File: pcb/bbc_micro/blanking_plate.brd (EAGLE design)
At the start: 66 x 45.5 mm, 0 parts

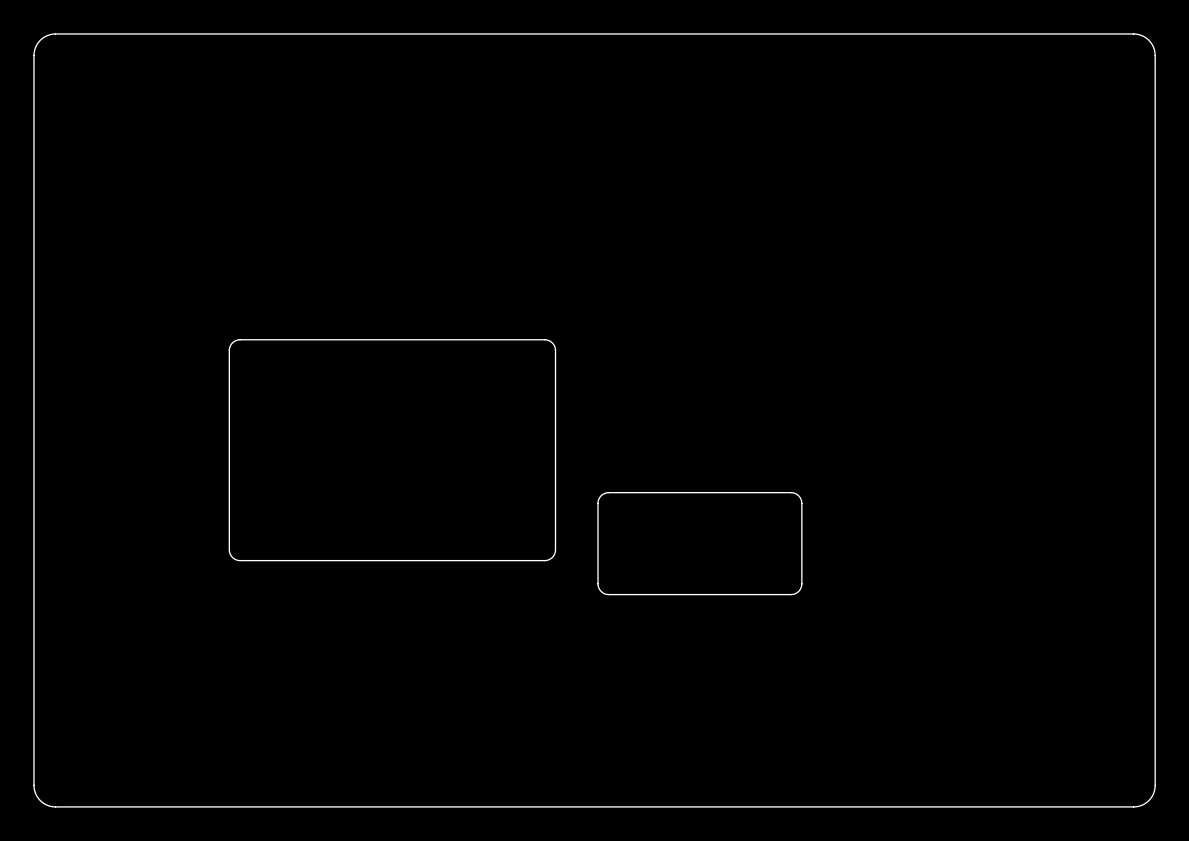
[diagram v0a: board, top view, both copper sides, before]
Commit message: added more caps
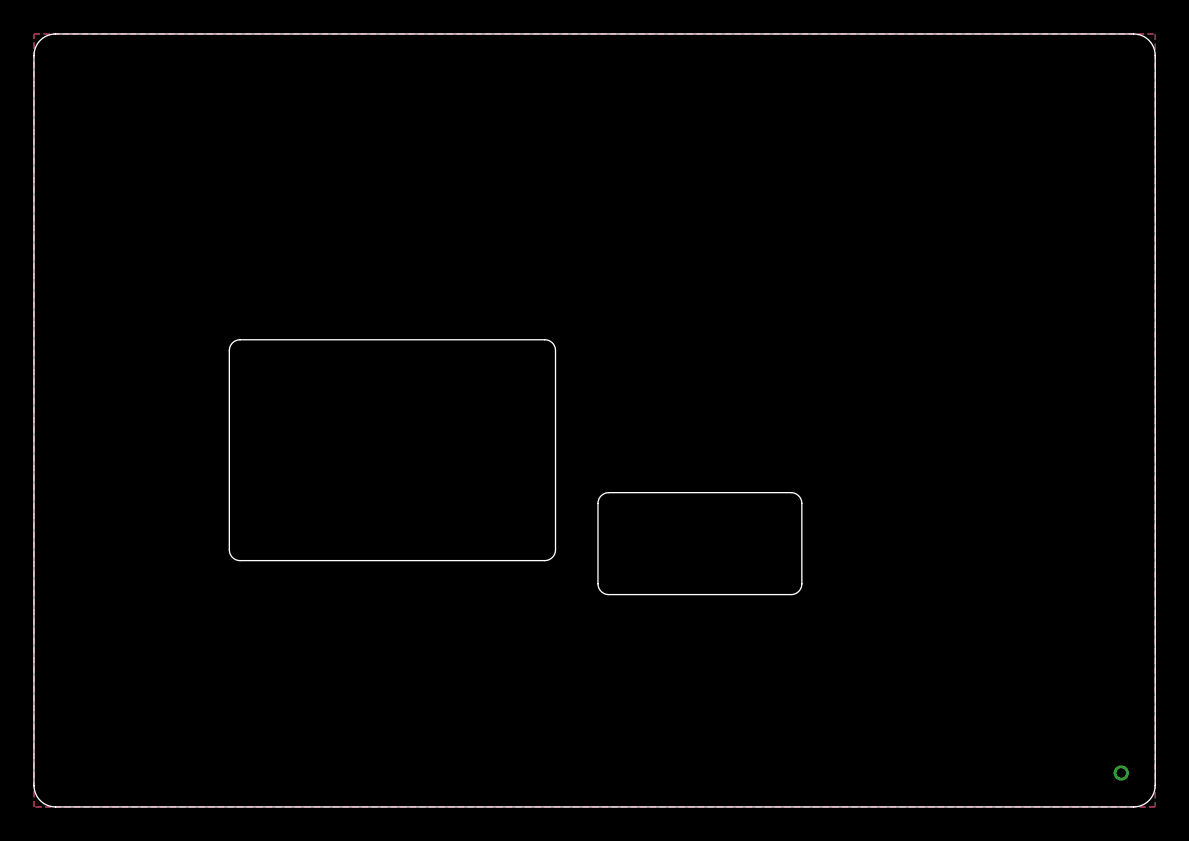
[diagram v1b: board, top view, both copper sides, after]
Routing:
- added copper zone on layer 1, net GND
- added copper zone on layer 16, net GND
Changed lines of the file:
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@@
 </elements>
 <signals>
+<signal name="GND">
+<polygon width="0" layer="1" isolate="0.6096">
+<vertex x="0" y="45"/>
+<vertex x="66" y="45"/>
+<vertex x="66" y="-0.5"/>
+<vertex x="0" y="-0.5"/>
+</polygon>
+<polygon width="0" layer="16" isolate="0.6096" thermals="no">
+<vertex x="0" y="45"/>
+<vertex x="66" y="45"/>
+<vertex x="66" y="-0.5"/>
+<vertex x="0" y="-0.5"/>
+</polygon>
+<via x="64" y="1.5" extent="1-16" drill="0.55"/>
+</signal>
 </signals>
 <mfgpreviewcolors>
